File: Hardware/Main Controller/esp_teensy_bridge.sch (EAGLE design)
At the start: 47 parts, among them IC1 BQ79600PWRQ1, Q1 SI7611DN-T1-GE3, Q2 SI7611DN-T1-GE3, Q3 SI7611DN-T1-GE3, Q4 SI7611DN-T1-GE3

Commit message: final additions hopefully
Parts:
- added LED1, LED2, LED3, LED4, LED5, LED6, LED7, LED8: (no value), led:LEDSML0603
- added R11, R12, R13, R14: 100k, rcl:R-US_R0603
- added R15, R16, R17, R18: 50, rcl:R-US_R0603
- added X1: 5566-12, con-molex:5566-12
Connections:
- new net N$13: LED4.A, R14.2
- new net N$14: U$3.14-A0/TX3/SPDIF_OUT, X1-1.S
- new net N$17: U$3.15-A1/RX3/SPDIF_IN, X1-2.S
- new net N$18: U$3.18-A4/SDA0, X1-3.S
- new net N$19: U$3.19-A5/SCL0, X1-4.S
- new net N$20: U$3.24-A10/TX6/SCL2, X1-5.S
- new net N$21: U$3.25-A11/RX6/SDA2, X1-6.S
- new net N$22: U$3.40-A16/CS1, X1-7.S
- new net N$23: U$3.32-OUT1B, X1-8.S
- new net N$24: U$3.9-OUT1C, X1-9.S
- new net N$25: U$3.6-OUT1D, X1-10.S
- new net N$26: U$3.33-MCLK2, X1-12.S
- new net N$27: U$3.2-OUT2, X1-11.S
- new net N$28: R15.1, U$2.IO19
- new net N$29: R16.1, U$2.IO18
- new net N$3: LED1.A, R11.2
- new net N$30: R17.1, U$2.IO5
- new net N$31: R18.1, U$2.IO17
- new net N$32: LED5.A, R15.2
- new net N$33: LED6.A, R16.2
- new net N$34: LED7.A, R17.2
- new net N$35: LED8.A, R18.2
- new net N$4: LED2.A, R12.2
- new net N$9: LED3.A, R13.2
- net GND: now also LED1.C, LED2.C, LED3.C, LED4.C, LED5.C, LED6.C, LED7.C, LED8.C
- net N$12: now also R12.1
- net N$2: now also R13.1
- net N$5: now also R14.1
- net N$6: now also R11.1
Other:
- moved on the sheet: CAN1-3, CAN1-4

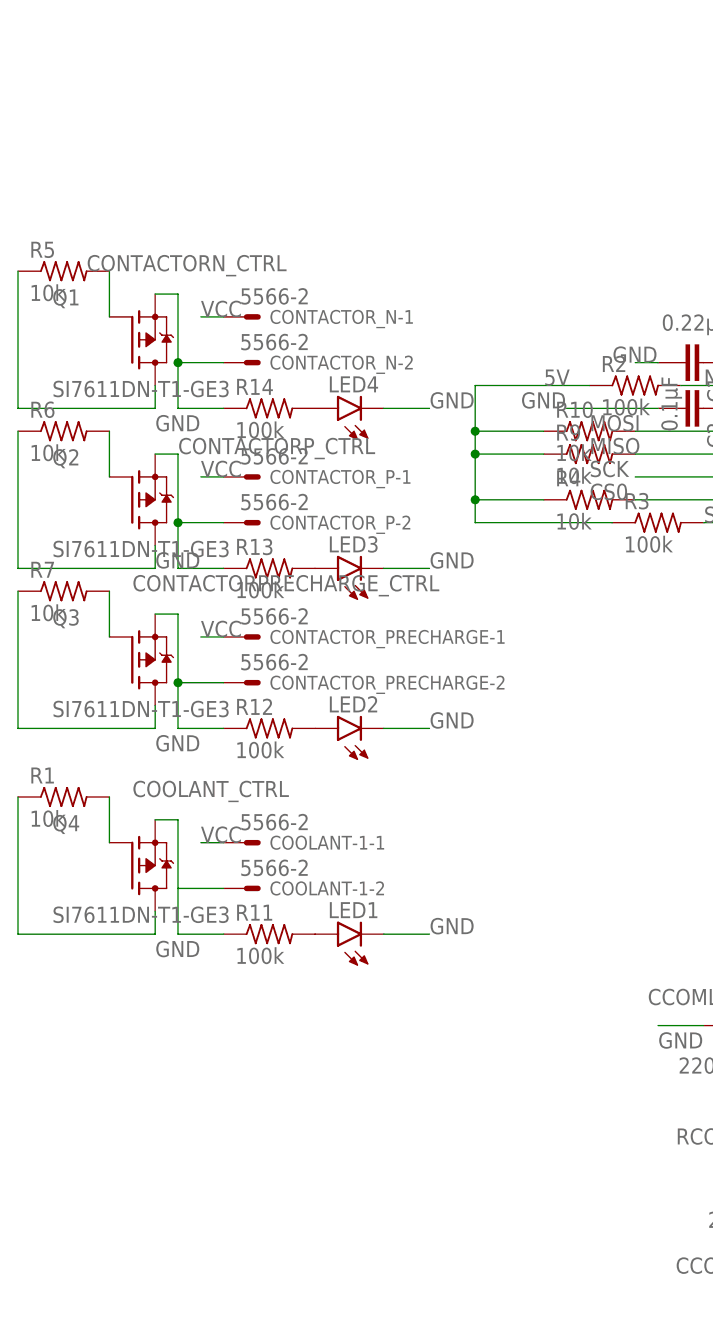
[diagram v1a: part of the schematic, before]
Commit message: Fixed MOSFETs
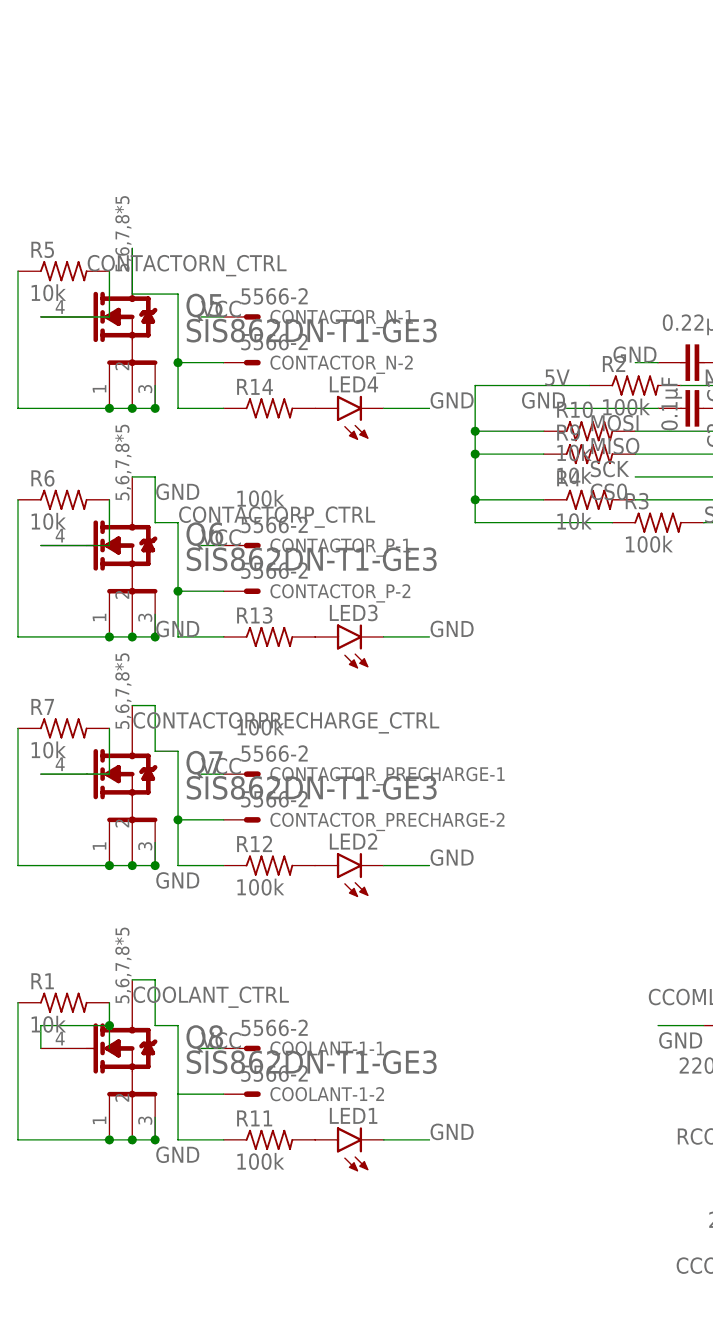
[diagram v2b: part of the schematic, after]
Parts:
- removed Q1, Q2, Q3, Q4: SI7611DN-T1-GE3, SI7611DN-T1-GE3:SI7611DN-T1-GE3
- added Q5, Q6, Q7, Q8: VISHAY_SIS862DN-T1-GE3VISHAY_SIS862DN-T1-GE3_0_0, Vishay - SIS862DN-T1-GE3:VISHAY_SIS862DN-T1-GE3VISHAY_SIS862DN-T1-GE3_0_0
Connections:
- net CONTACTORN_CTRL: now also Q5.G; no longer Q1.G
- net CONTACTORPRECHARGE_CTRL: now also Q7.G; no longer Q3.G
- net CONTACTORP_CTRL: now also Q6.G; no longer Q2.G
- net COOLANT_CTRL: now also Q8.G; no longer Q4.G
- net GND: now also Q5.1_S, Q5.2_S, Q5.3_S, Q6.1_S, Q6.2_S, Q6.3_S, Q7.1_S, Q7.2_S, Q7.3_S, Q8.1_S, Q8.2_S, Q8.3_S; no longer Q1.D, Q2.D, Q3.D, Q4.D
- net N$12: now also Q7.D; no longer Q3.S
- net N$2: now also Q6.D; no longer Q2.S
- net N$5: now also Q5.D; no longer Q1.S
- net N$6: now also Q8.D; no longer Q4.S
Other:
- moved on the sheet: CONTACTOR_P-1, CONTACTOR_P-2, CONTACTOR_PRECHARGE-1, CONTACTOR_PRECHARGE-2, COOLANT-1-1, COOLANT-1-2, LED1, LED2, LED3, R1, R11, R12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

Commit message: Fixed LED issue
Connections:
- net CONTACTORN_CTRL: now also R14.1
- net CONTACTORPRECHARGE_CTRL: now also R12.1
- net CONTACTORP_CTRL: now also R13.1
- net COOLANT_CTRL: now also R11.1
- net N$12: no longer R12.1
- net N$2: no longer R13.1
- net N$5: no longer R14.1
- net N$6: no longer R11.1
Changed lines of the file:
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@@
 <pinref part="Q5" gate="G$0" pin="G"/>
 <wire x1="-134.62" y1="71.12" x2="-142.24" y2="71.12" width="0.1524" layer="91"/>
+<pinref part="R14" gate="G$1" pin="1"/>
+<wire x1="-127" y1="60.96" x2="-121.92" y2="60.96" width="0.1524" layer="91"/>
+<wire x1="-127" y1="60.96" x2="-127" y2="71.12" width="0.1524" layer="91"/>
+<wire x1="-127" y1="71.12" x2="-142.24" y2="71.12" width="0.1524" layer="91"/>
+<junction x="-142.24" y="71.12"/>
 </segment>
 <segment>
@@
 <pinref part="CONTACTOR_N" gate="-2" pin="S"/>
 <wire x1="-127" y1="66.04" x2="-121.92" y2="66.04" width="0.1524" layer="91"/>
-<pinref part="R14" gate="G$1" pin="1"/>
-<wire x1="-127" y1="66.04" x2="-127" y2="60.96" width="0.1524" layer="91"/>
-<wire x1="-127" y1="60.96" x2="-121.92" y2="60.96" width="0.1524" layer="91"/>
-<junction x="-127" y="66.04"/>
 <pinref part="Q5" gate="G$0" pin="D"/>
 <wire x1="-132.08" y1="78.74" x2="-132.08" y2="73.66" width="0.1524" layer="91"/>
@@
 <wire x1="-127" y1="48.26" x2="-127" y2="40.64" width="0.1524" layer="91"/>
 <wire x1="-127" y1="40.64" x2="-121.92" y2="40.64" width="0.1524" layer="91"/>
-<pinref part="R13" gate="G$1" pin="1"/>
-<wire x1="-127" y1="40.64" x2="-127" y2="35.56" width="0.1524" layer="91"/>
-<wire x1="-127" y1="35.56" x2="-121.92" y2="35.56" width="0.1524" layer="91"/>
-<junction x="-127" y="40.64"/>
 <pinref part="Q6" gate="G$0" pin="D"/>
 <wire x1="-129.54" y1="48.26" x2="-129.54" y2="53.34" width="0.1524" layer="91"/>
@@
 <pinref part="Q6" gate="G$0" pin="G"/>
 <wire x1="-134.62" y1="45.72" x2="-142.24" y2="45.72" width="0.1524" layer="91"/>
+<pinref part="R13" gate="G$1" pin="1"/>
+<wire x1="-127" y1="35.56" x2="-121.92" y2="35.56" width="0.1524" layer="91"/>
+<wire x1="-127" y1="35.56" x2="-127" y2="45.72" width="0.1524" layer="91"/>
+<wire x1="-127" y1="45.72" x2="-142.24" y2="45.72" width="0.1524" layer="91"/>
+<junction x="-142.24" y="45.72"/>
 </segment>
 <segment>
@@
 <pinref part="Q7" gate="G$0" pin="G"/>
 <wire x1="-134.62" y1="20.32" x2="-142.24" y2="20.32" width="0.1524" layer="91"/>
+<pinref part="R12" gate="G$1" pin="1"/>
+<wire x1="-127" y1="10.16" x2="-121.92" y2="10.16" width="0.1524" layer="91"/>
+<wire x1="-127" y1="10.16" x2="-127" y2="20.32" width="0.1524" layer="91"/>
+<wire x1="-127" y1="20.32" x2="-142.24" y2="20.32" width="0.1524" layer="91"/>
+<junction x="-142.24" y="20.32"/>
 </segment>
 <segment>
@@
 <pinref part="CONTACTOR_PRECHARGE" gate="-2" pin="S"/>
 <wire x1="-127" y1="15.24" x2="-121.92" y2="15.24" width="0.1524" layer="91"/>
-<pinref part="R12" gate="G$1" pin="1"/>
-<wire x1="-127" y1="15.24" x2="-127" y2="10.16" width="0.1524" layer="91"/>
-<wire x1="-127" y1="10.16" x2="-121.92" y2="10.16" width="0.1524" layer="91"/>
-<junction x="-127" y="15.24"/>
 <pinref part="Q7" gate="G$0" pin="D"/>
 <wire x1="-129.54" y1="22.86" x2="-129.54" y2="27.94" width="0.1524" layer="91"/>
@@
 <pinref part="COOLANT-1" gate="-2" pin="S"/>
 <wire x1="-121.92" y1="-15.24" x2="-127" y2="-15.24" width="0.1524" layer="91"/>
-<wire x1="-127" y1="-15.24" x2="-127" y2="-20.32" width="0.1524" layer="91"/>
-<wire x1="-127" y1="-20.32" x2="-121.92" y2="-20.32" width="0.1524" layer="91"/>
-<pinref part="R11" gate="G$1" pin="1"/>
 <pinref part="Q8" gate="G$0" pin="D"/>
 <wire x1="-129.54" y1="-7.62" x2="-129.54" y2="-2.54" width="0.1524" layer="91"/>
@@
 <wire x1="-142.24" y1="-7.62" x2="-142.24" y2="-10.16" width="0.1524" layer="91"/>
 <junction x="-134.62" y="-7.62"/>
+<wire x1="-127" y1="-20.32" x2="-121.92" y2="-20.32" width="0.1524" layer="91"/>
+<pinref part="R11" gate="G$1" pin="1"/>
+<wire x1="-127" y1="-20.32" x2="-127" y2="-10.16" width="0.1524" layer="91"/>
+<wire x1="-127" y1="-10.16" x2="-142.24" y2="-10.16" width="0.1524" layer="91"/>
+<junction x="-142.24" y="-10.16"/>
 </segment>
 <segment>

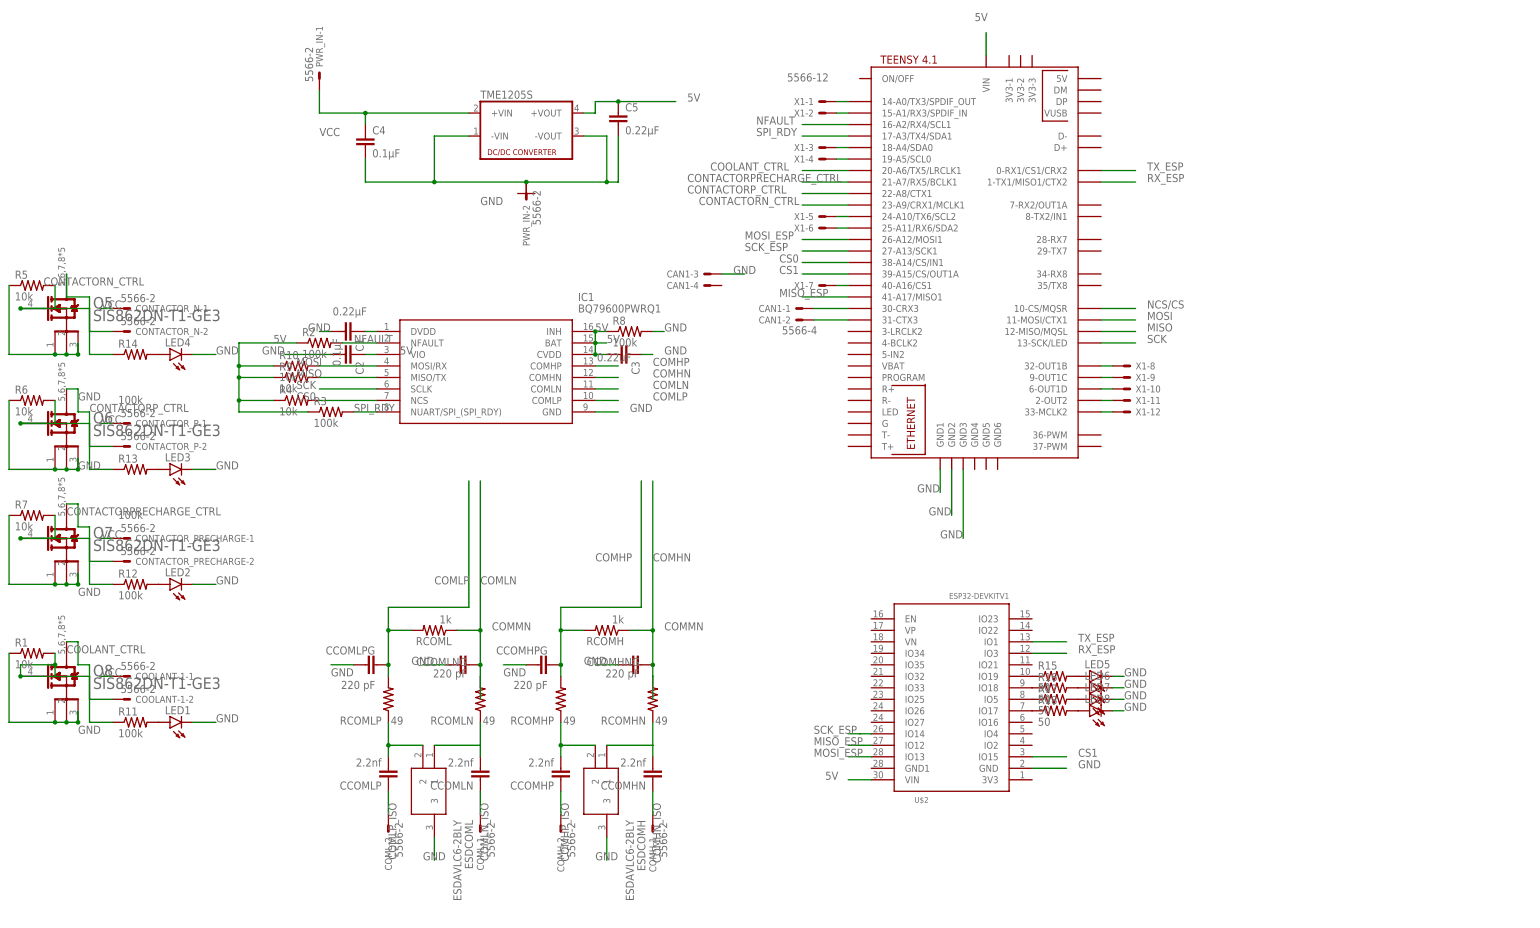
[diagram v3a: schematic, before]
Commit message: Fixed LED VCC and resistors, coolant is now PWM, CAN transceiver added, removed unnecessary resistor
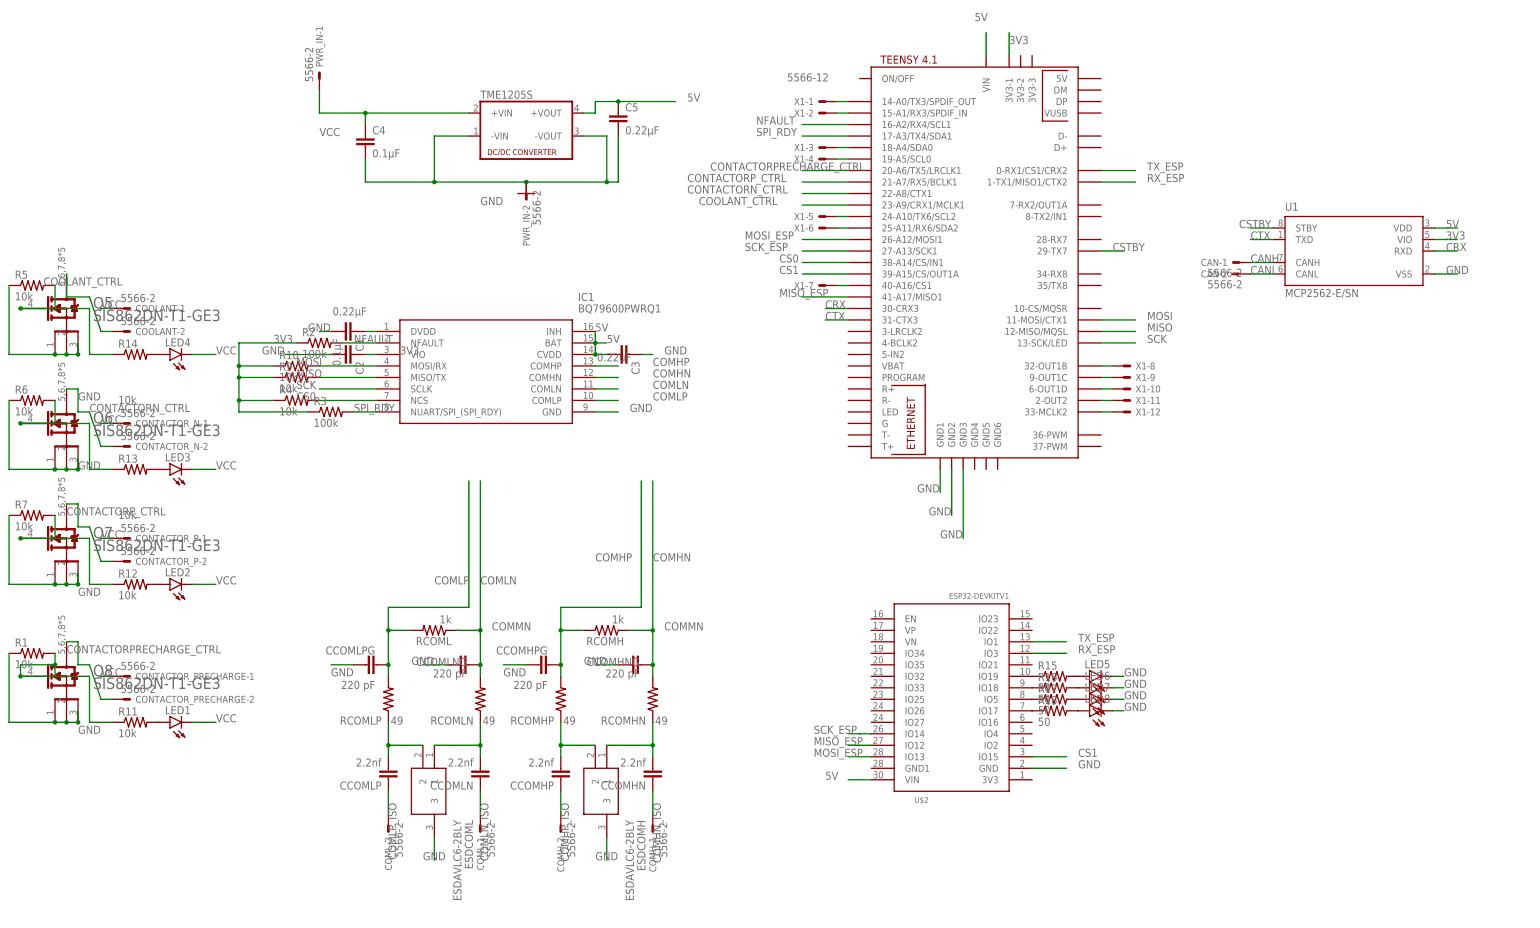
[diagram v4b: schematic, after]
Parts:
- removed CAN1: 5566-4, con-molex:5566-4
- removed COOLANT-1: 5566-2, con-molex:5566-2
- removed R8: 100k, rcl:R-US_R0603
- added CAN, COOLANT: 5566-2, con-molex:5566-2
- added U1: MCP2562-E/SN, MCP2562-E_SN:MCP2562-E/SN
- R11, R12, R13, R14: value 100k -> 10k
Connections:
- removed net N$7: CAN1-1.S, U$3.30-CRX3
- removed net N$8: CAN1-2.S, U$3.31-CTX3
- removed net NCS/CS: U$3.10-CS/MQSR
- new net 3V3: C2.1, IC1.VIO, R10.1, R2.1, R3.1, R4.1, R9.1, U$3.3V3-1, U1.VIO
- new net CANH: CAN-1.S, U1.CANH
- new net CANL: CAN-2.S, U1.CANL
- new net CRX: U$3.30-CRX3, U1.RXD
- new net CSTBY: U$3.29-TX7, U1.STBY
- new net CTX: U$3.31-CTX3, U1.TXD
- net 5V: now also U1.VDD; no longer C2.1, IC1.VIO, R10.1, R2.1, R3.1, R4.1, R8.1, R9.1
- net CONTACTORN_CTRL: now also Q6.G, R13.1, R6.2, U$3.22-A8/CTX1; no longer Q5.G, R14.1, R5.2, U$3.23-A9/CRX1/MCLK1
- net CONTACTORPRECHARGE_CTRL: now also Q8.G, R1.2, R11.1, U$3.20-A6/TX5/LRCLK1; no longer Q7.G, R12.1, R7.2, U$3.21-A7/RX5/BCLK1
- net CONTACTORP_CTRL: now also Q7.G, R12.1, R7.2, U$3.21-A7/RX5/BCLK1; no longer Q6.G, R13.1, R6.2, U$3.22-A8/CTX1
- net COOLANT_CTRL: now also Q5.G, R14.1, R5.2, U$3.23-A9/CRX1/MCLK1; no longer Q8.G, R1.2, R11.1, U$3.20-A6/TX5/LRCLK1
- net GND: now also U1.VSS; no longer CAN1-3.S, LED1.C, LED2.C, LED3.C, LED4.C, R8.2
- net N$12: now also CONTACTOR_P-2.S; no longer CONTACTOR_PRECHARGE-2.S
- net N$2: now also CONTACTOR_N-2.S; no longer CONTACTOR_P-2.S
- net N$5: now also COOLANT-2.S; no longer CONTACTOR_N-2.S
- net N$6: now also CONTACTOR_PRECHARGE-2.S; no longer COOLANT-1-2.S
- net VCC: now also COOLANT-1.S, LED1.C, LED2.C, LED3.C, LED4.C; no longer COOLANT-1-1.S
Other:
- moved on the sheet: CONTACTOR_N-1, CONTACTOR_N-2, CONTACTOR_P-1, CONTACTOR_P-2, CONTACTOR_PRECHARGE-1, CONTACTOR_PRECHARGE-2
